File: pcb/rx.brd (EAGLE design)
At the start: 19 x 38 mm, 34 parts, among them Y1 CRYSTAL-26MHZSMD-3.2X2.5

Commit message: rev3 working
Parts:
- C1, C14, C2: value 100nF -> 4.7uF
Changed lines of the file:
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@@
 <element name="U$3" library="nRF24L01-Chip-v13" package="QFN20_ALT1" value="NRF24L01ALT1" x="5.969" y="22.543" smashed="yes" rot="R90"/>
 <element name="U$1" library="3pos_slide_switch" package="SW_3POS_FOOT_OFFICIAL" value="SW_3POS_DEVSW_3POS_OFFICIAL" x="0.7016" y="12.746" smashed="yes" rot="R270"/>
-<element name="C1" library="clock" package="0805" value="100nF" x="1.905" y="23.305" smashed="yes" rot="R180">
+<element name="C1" library="clock" package="0805" value="4.7uF" x="1.905" y="23.305" smashed="yes" rot="R180">
 <attribute name="NAME" x="2.0828" y="28.3215" size="0.8128" layer="25" rot="R180"/>
 </element>
@@
 <attribute name="NAME" x="2.2352" y="30.0614" size="0.8128" layer="25" rot="R180"/>
 </element>
-<element name="C2" library="clock" package="0805" value="100nF" x="1.905" y="26.607" smashed="yes" rot="R180">
+<element name="C2" library="clock" package="0805" value="4.7uF" x="1.905" y="26.607" smashed="yes" rot="R180">
 <attribute name="NAME" x="2.0574" y="31.56" size="0.8128" layer="25" rot="R180"/>
 </element>
@@
 <attribute name="VALUE" x="0.889" y="18.606" size="0.4064" layer="27"/>
 </element>
-<element name="C14" library="clock" package="0805" value="100nF" x="1.905" y="18.352" smashed="yes" rot="R180">
+<element name="C14" library="clock" package="0805" value="4.7uF" x="1.905" y="18.352" smashed="yes" rot="R180">
 <attribute name="NAME" x="2.3876" y="15.3929" size="0.8128" layer="25" rot="R180"/>
 </element>

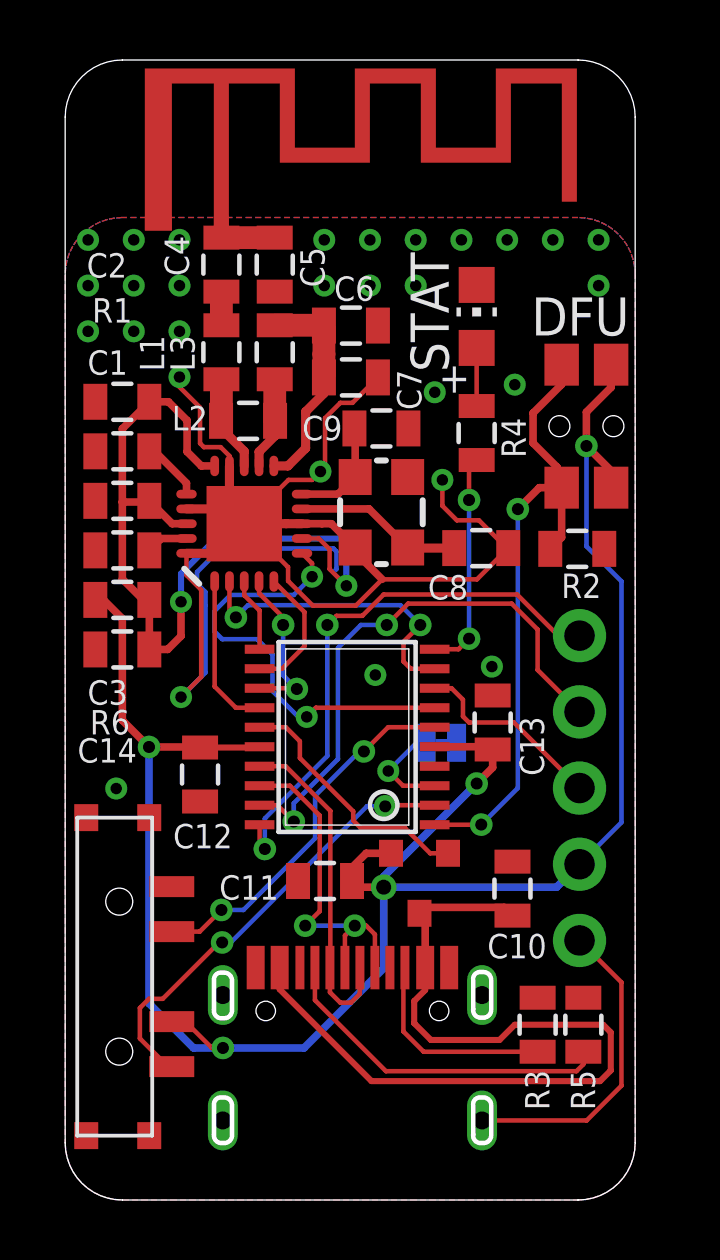
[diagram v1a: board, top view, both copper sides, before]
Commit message: tx board removed jumper
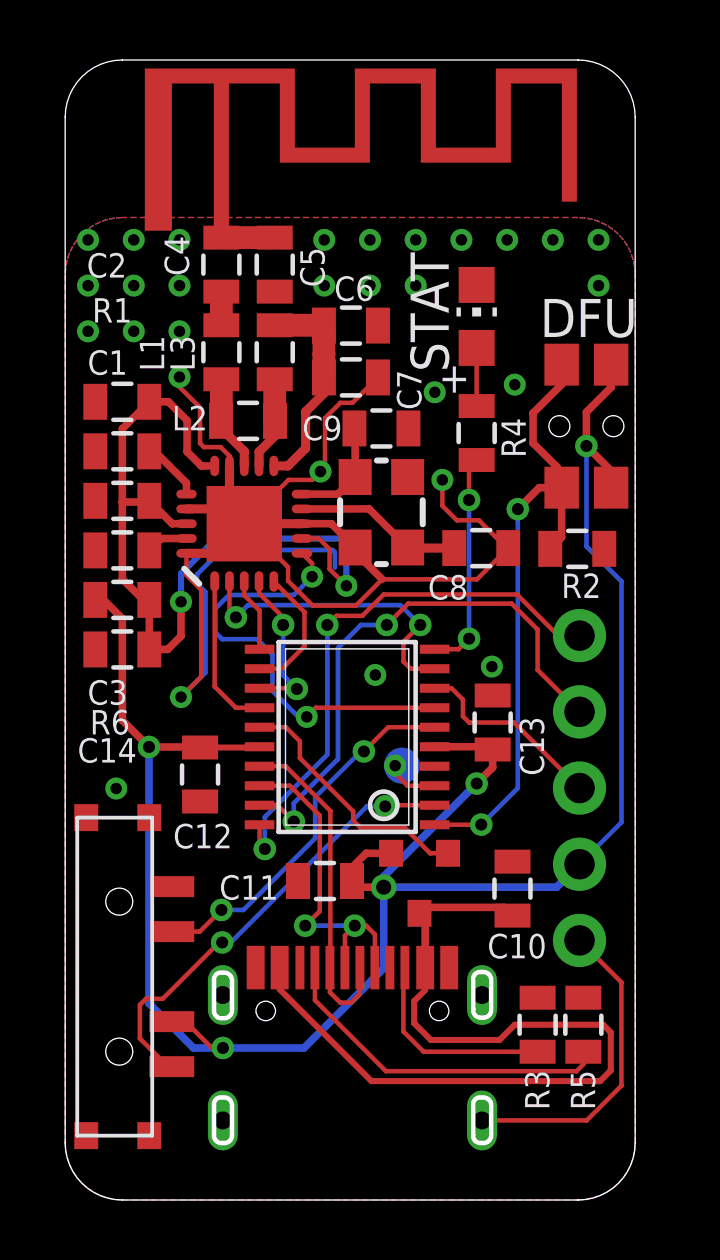
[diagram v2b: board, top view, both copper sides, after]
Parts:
- removed SJ1: JUMPER-SMT_2_NC_TRACE_NO-SILK, SparkFun-Jumpers:SMT-JUMPER_2_NC_TRACE_NO-SILK
- added TP2: TPTP12R, testpad:TP12R
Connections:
- net GND: no longer SJ1.1
- net N$19: now also TP2.TP; no longer SJ1.2
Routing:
- net N$19: track 3.40 -> 1.74 mm
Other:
- board text added: "PF1"
- board text added: "REV4 MAY15 19"
- board text removed: "CH"
- board text removed: "REV3 FEB25 19"

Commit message: before trail run
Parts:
- C3: value 33nF -> 100nF
- C8, C9: value 22pF -> 12pF
- Y1: value CRYSTAL-26MHZSMD-3.2X2.5 -> 16MHz_12pF
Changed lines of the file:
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@@
 <attribute name="NAME" x="2.0574" y="31.56" size="0.8128" layer="25" rot="R180"/>
 </element>
-<element name="C3" library="clock" package="0805" value="33nF" x="1.905" y="21.654" smashed="yes" rot="R180">
+<element name="C3" library="clock" package="0805" value="100nF" x="1.905" y="21.654" smashed="yes" rot="R180">
 <attribute name="NAME" x="2.0828" y="17.3233" size="0.8128" layer="25" rot="R180"/>
 </element>
@@
 <attribute name="NAME" x="11.0617" y="27.6738" size="0.8128" layer="25" rot="R270"/>
 </element>
-<element name="C8" library="clock" package="0805" value="22pF" x="13.8684" y="21.7302" smashed="yes">
+<element name="C8" library="clock" package="0805" value="12pF" x="13.8684" y="21.7302" smashed="yes">
 <attribute name="NAME" x="12.0904" y="20.0157" size="0.8128" layer="25"/>
 </element>
-<element name="C9" library="clock" package="0805" value="22pF" x="10.541" y="25.718" smashed="yes">
+<element name="C9" library="clock" package="0805" value="12pF" x="10.541" y="25.718" smashed="yes">
 <attribute name="NAME" x="7.8994" y="25.3243" size="0.8128" layer="25"/>
 </element>
@@
 <attribute name="NAME" x="7.112" y="10.8237" size="0.8128" layer="25" rot="R180"/>
 </element>
-<element name="Y1" library="SparkFun-Clocks" package="CRYSTAL-SMD-3.2X2.5MM" value="CRYSTAL-26MHZSMD-3.2X2.5" x="10.541" y="22.924" smashed="yes" rot="R90">
+<element name="Y1" library="SparkFun-Clocks" package="CRYSTAL-SMD-3.2X2.5MM" value="16MHz_12pF" x="10.541" y="22.924" smashed="yes" rot="R90">
 <attribute name="PROD_ID" value="XTAL-12454" x="10.541" y="22.924" size="1.778" layer="27" rot="R90" display="off"/>
 </element>

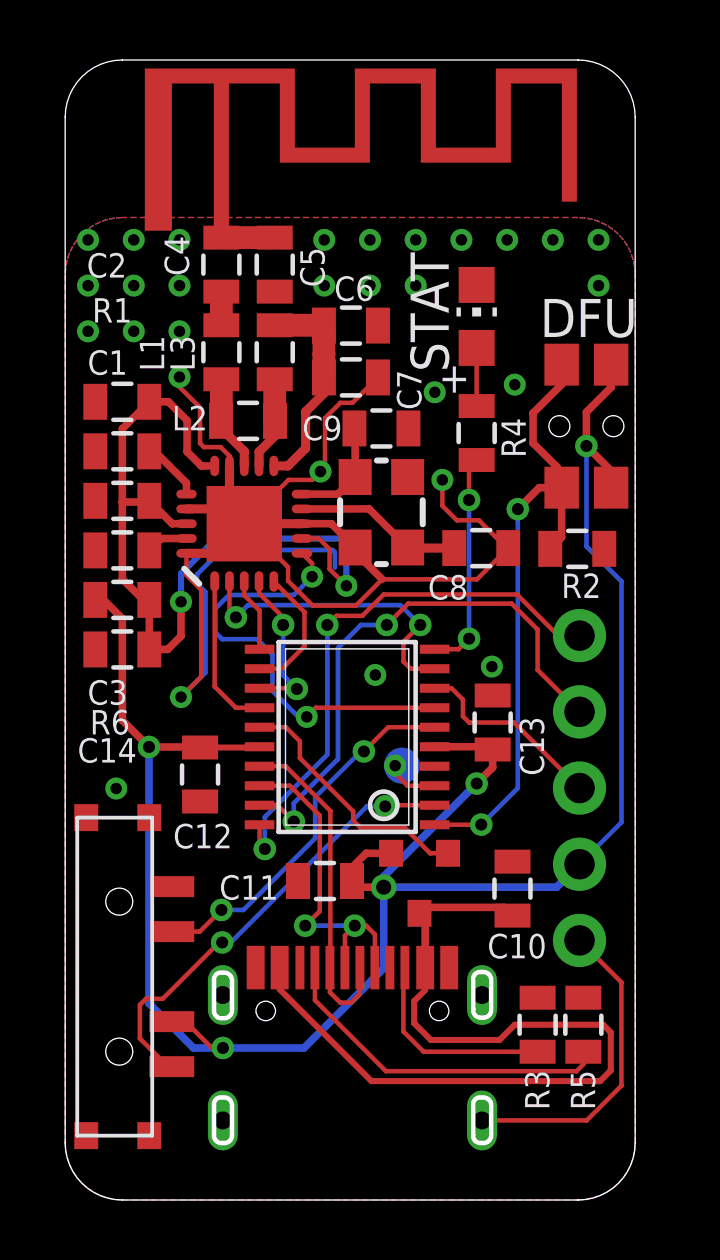
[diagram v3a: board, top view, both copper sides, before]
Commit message: centered usbc footprint, adjusted board layout
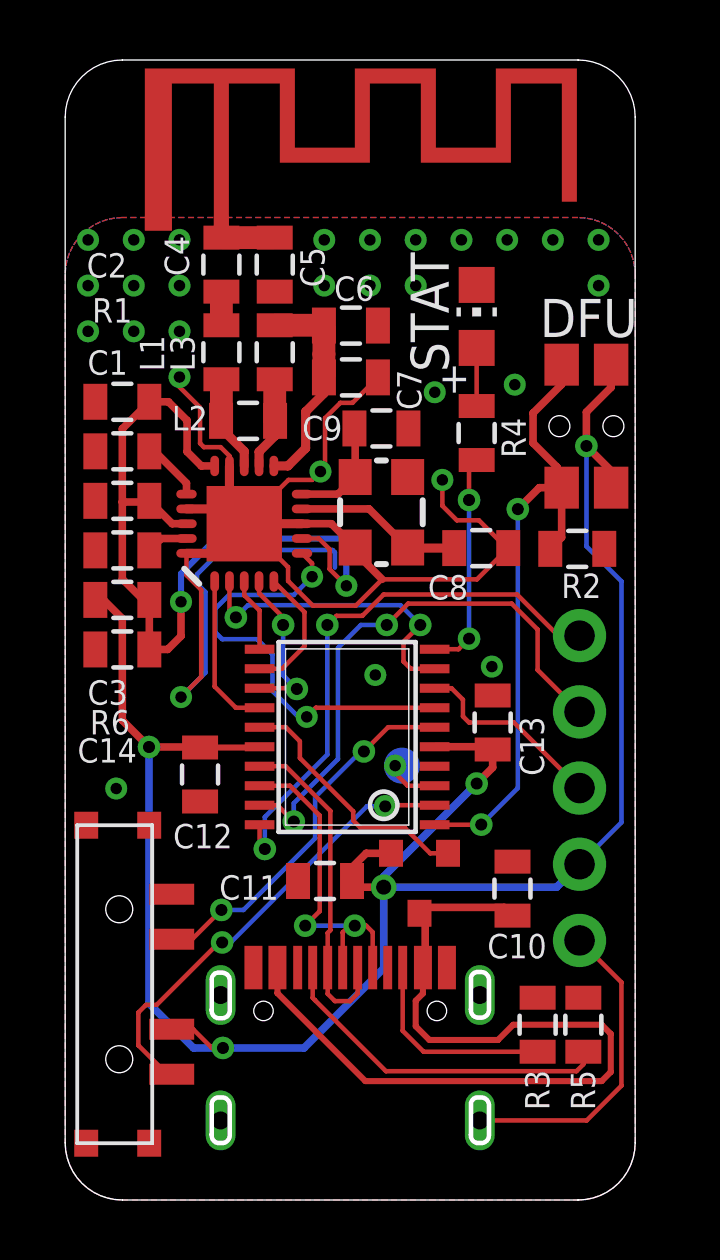
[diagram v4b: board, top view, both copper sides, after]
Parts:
- removed U$6: USBC_16P, my_usbc_16p:USBC_16P_FOOT
- added U$7: USBC_16P_CENTERED, my_usbc_16p_centered:USBC_16P_FOOT
- moved U$1 0.25 mm to (0.70, 12.5)
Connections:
- net +5V: now also U$7.A4B9, U$7.B4A9; no longer U$6.A4B9, U$6.B4A9
- net GND: now also U$7.A1B12, U$7.B11A12, U$7.P$13, U$7.P$14, U$7.P$15, U$7.P$16; no longer U$6.A1B12, U$6.B11A12, U$6.P$13, U$6.P$14, U$6.P$15, U$6.P$16
- net N$12: now also U$7.A7, U$7.B7; no longer U$6.A7, U$6.B7
- net N$13: now also U$7.A6, U$7.B6; no longer U$6.A6, U$6.B6
- net N$25: now also U$7.B5; no longer U$6.B5
- net N$27: now also U$7.A5; no longer U$6.A5
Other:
- board text added: "PD1 190523"
- board text removed: "REV4 MAY15 19"

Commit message: foodprint adjustment, coord file
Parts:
- removed U$1: SW_3POS_DEVSW_3POS_OFFICIAL, 3pos_slide_switch:SW_3POS_FOOT_OFFICIAL
- added SW1: SW_3POS_DEVSW_3POS_OFFICIAL, 3pos_slide_switch_centered:SW_3POS_FOOT_OFFICIAL
- renumbered U$10 to SW2, U$2 to IC1, U$3 to IC2, U$4 to U2, U$7 to U1
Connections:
- net +3V3: now also SW1.P$7; no longer U$1.P$7
- net GND: now also SW1.P$1, SW1.P$2, SW1.P$4, SW1.P$5; no longer U$1.P$1, U$1.P$2, U$1.P$4, U$1.P$5
- net N$10: now also SW1.P$8; no longer U$1.P$8
- net N$26: now also SW1.P$6; no longer U$1.P$6

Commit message: adjusted timing budget, distance under 15mm are now ignored
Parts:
- renumbered LED2 to LED1
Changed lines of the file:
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@@
 </element>
 <element name="SW2" library="3pos_slide_switch" package="342_SWICH_FOOT_HOLE" value="324_SW324_SWITCH_FOOT_HOLE" x="17.3736" y="25.7942" smashed="yes" rot="R90"/>
-<element name="LED2" library="joyAnalog" package="CHIP-LED0805" value="" x="13.716" y="29.4518" smashed="yes">
+<element name="LED1" library="joyAnalog" package="CHIP-LED0805" value="" x="13.716" y="29.4518" smashed="yes">
 <attribute name="VALUE" x="16.256" y="28.1818" size="1.27" layer="27" rot="R90"/>
 <attribute name="VALUE" x="16.256" y="28.1818" size="1.27" layer="27" rot="R90"/>
@@
 <wire x1="9.666" y1="21.749" x2="8.872" y2="22.543" width="0.254" layer="1"/>
 <wire x1="8.872" y1="22.543" x2="7.8944" y2="22.543" width="0.254" layer="1"/>
-<contactref element="LED2" pad="C"/>
+<contactref element="LED1" pad="C"/>
 <wire x1="14.7684" y1="21.7302" x2="13.727" y2="20.6888" width="0.1524" layer="1"/>
 <wire x1="13.727" y1="20.6888" x2="10.5664" y2="20.6888" width="0.1524" layer="1"/>
@@
 <signal name="N$18">
 <contactref element="R4" pad="1"/>
-<contactref element="LED2" pad="A"/>
+<contactref element="LED1" pad="A"/>
 <wire x1="13.716" y1="28.4018" x2="13.716" y2="26.4656" width="0.1524" layer="1"/>
 </signal>

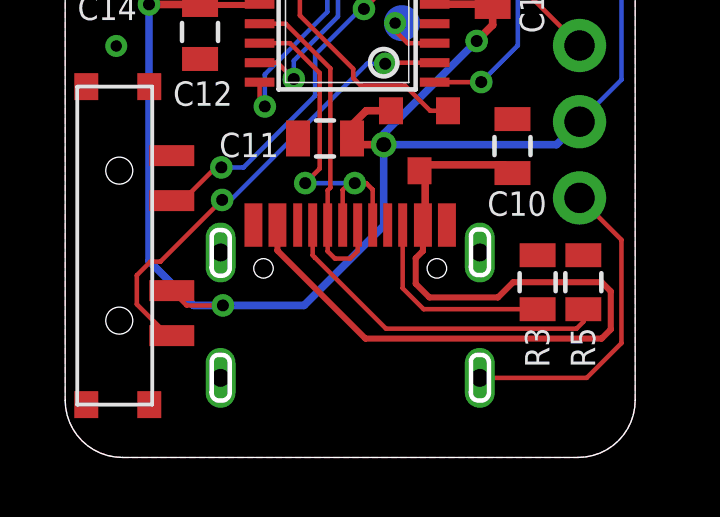
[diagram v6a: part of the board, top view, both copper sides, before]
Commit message: updated USBC connector, check_battery DBZ
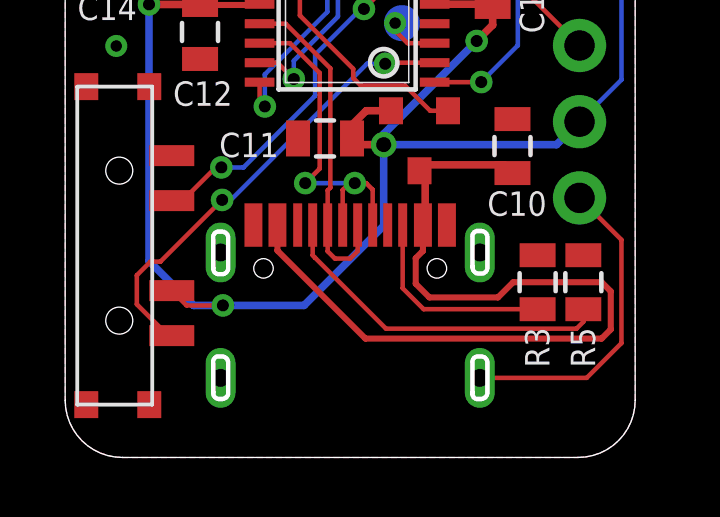
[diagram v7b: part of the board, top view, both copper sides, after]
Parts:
- U1: value USBC_16P_CENTERED -> USBC_16P; device my_usbc_16p_centered:USBC_16P_FOOT -> my_usbc_16p:USBC_16P_FOOT
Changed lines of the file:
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@@
 <layer number="44" name="Drills" color="7" fill="1" visible="no" active="yes"/>
 <layer number="45" name="Holes" color="7" fill="1" visible="no" active="yes"/>
-<layer number="46" name="Milling" color="3" fill="1" visible="no" active="yes"/>
+<layer number="46" name="Milling" color="3" fill="1" visible="yes" active="yes"/>
 <layer number="47" name="Measures" color="7" fill="1" visible="no" active="yes"/>
 <layer number="48" name="Document" color="7" fill="1" visible="no" active="yes"/>
@@
 <attribute name="VALUE" x="11.7348" y="13.843" size="0.0254" layer="28" rot="MR0"/>
 </element>
-<element name="U1" library="my_usbc_16p_centered" package="USBC_16P_FOOT" value="USBC_16P_CENTERED" x="9.5" y="3.9"/>
+<element name="U1" library="my_usbc_16p" package="USBC_16P_FOOT" value="USBC_16P" x="9.5" y="3.9"/>
 <element name="SW1" library="3pos_slide_switch_centered" package="SW_3POS_FOOT_OFFICIAL" value="SW_3POS_DEVSW_3POS_OFFICIAL" x="1.7526" y="7.0612" rot="R270"/>
 </elements>
